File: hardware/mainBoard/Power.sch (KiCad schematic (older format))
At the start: 70 parts

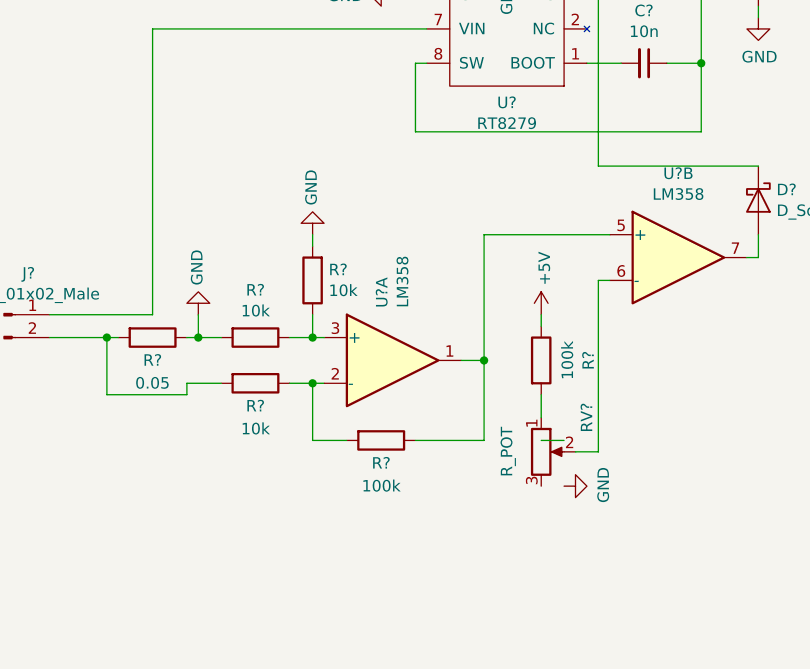
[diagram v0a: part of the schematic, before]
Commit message: Added external connections, analog conditioning and several items
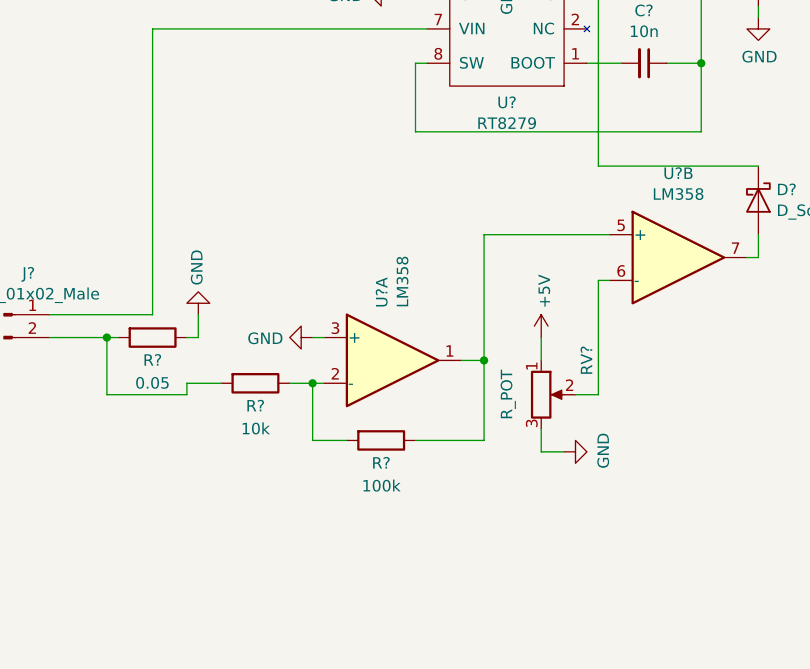
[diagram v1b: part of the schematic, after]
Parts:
- removed R? (x2): 10k, symbol Device:R
- removed R?: 100k, symbol Device:R
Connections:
- net +5V: now also RV?.1
- net GND: now also RV?.3, U?.3 (+)
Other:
- moved on the sheet: RV?
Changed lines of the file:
@@
 EESchema Schematic File Version 4
+LIBS:prockeckv2-cache
 EELAYER 30 0
 EELAYER END
 $Descr A4 11693 8268
 encoding utf-8
-Sheet 5 5
+Sheet 4 8
 Title ""
 Date ""
@@
 	8200 5350 8250 5350
 Wire Wire Line
-	8200 6100 8200 5350
-Wire Wire Line
-	8100 6100 8200 6100
+	8200 5850 8200 5350
+Wire Wire Line
+	8100 5850 8200 5850
 Wire Wire Line
 	6250 4250 7450 4250
-Wire Wire Line
-	7950 5550 7950 5500
-Wire Wire Line
-	7950 5950 7950 5850
-Wire Wire Line
-	8050 6050 7950 6050
 $Comp
 L power:GND #PWR?
 U 1 1 5E4F0960
-P 8050 6250
-F 0 "#PWR?" H 8050 6000 50  0001 C CNN
-F 1 "GND" H 8055 6077 50  0000 C CNN
-F 2 "" H 8050 6250 50  0001 C CNN
-F 3 "" H 8050 6250 50  0001 C CNN
-	1    8050 6250
+P 8050 6100
+F 0 "#PWR?" H 8050 5850 50  0001 C CNN
+F 1 "GND" H 8055 5927 50  0000 C CNN
+F 2 "" H 8050 6100 50  0001 C CNN
+F 3 "" H 8050 6100 50  0001 C CNN
+	1    8050 6100
 	0    -1   -1   0
 $EndComp
@@
 L Device:R_POT RV?
 U 1 1 5E4DE4A3
-P 7950 6100
-F 0 "RV?" V 8150 6250 50  0000 C CNN
-F 1 "R_POT" V 7800 6100 50  0000 C CNN
-F 2 "" H 7950 6100 50  0001 C CNN
-F 3 "~" H 7950 6100 50  0001 C CNN
-	1    7950 6100
-	1    0    0    -1
-$EndComp
-$Comp
-L Device:R R?
-U 1 1 5E4DD69F
-P 7950 5700
-F 0 "R?" V 8157 5700 50  0000 C CNN
-F 1 "100k" V 8066 5700 50  0000 C CNN
-F 2 "" V 7880 5700 50  0001 C CNN
-F 3 "~" H 7950 5700 50  0001 C CNN
-	1    7950 5700
+P 7950 5850
+F 0 "RV?" V 8150 6000 50  0000 C CNN
+F 1 "R_POT" V 7800 5850 50  0000 C CNN
+F 2 "" H 7950 5850 50  0001 C CNN
+F 3 "~" H 7950 5850 50  0001 C CNN
+	1    7950 5850
 	1    0    0    -1
 $EndComp
@@
 L power:+5V #PWR?
 U 1 1 5E4CA2F2
-P 7950 5500
-F 0 "#PWR?" H 7950 5350 50  0001 C CNN
-F 1 "+5V" V 7965 5628 50  0000 L CNN
-F 2 "" H 7950 5500 50  0001 C CNN
-F 3 "" H 7950 5500 50  0001 C CNN
-	1    7950 5500
+P 7950 5600
+F 0 "#PWR?" H 7950 5450 50  0001 C CNN
+F 1 "+5V" V 7965 5728 50  0000 L CNN
+F 2 "" H 7950 5600 50  0001 C CNN
+F 3 "" H 7950 5600 50  0001 C CNN
+	1    7950 5600
 	1    0    0    -1
 $EndComp
@@
 $EndComp
 Wire Wire Line
-	6450 5600 6550 5600
-Connection ~ 6450 5600
-Wire Wire Line
 	6450 5500 6450 5600
 $Comp
@@
 Wire Wire Line
 	5800 5500 6250 5500
-Wire Wire Line
-	6950 5150 6950 5200
 $Comp
 L power:GND #PWR?
 U 1 1 5E346CB4
-P 6950 5150
-F 0 "#PWR?" H 6950 4900 50  0001 C CNN
-F 1 "GND" V 6955 5022 50  0000 R CNN
-F 2 "" H 6950 5150 50  0001 C CNN
-F 3 "" H 6950 5150 50  0001 C CNN
-	1    6950 5150
-	-1   0    0    1
-$EndComp
-Wire Wire Line
-	6950 5600 7000 5600
-Connection ~ 6950 5600
-Wire Wire Line
-	6950 5500 6950 5600
-Wire Wire Line
-	6850 5600 6950 5600
+P 6950 5600
+F 0 "#PWR?" H 6950 5350 50  0001 C CNN
+F 1 "GND" V 6955 5472 50  0000 R CNN
+F 2 "" H 6950 5600 50  0001 C CNN
+F 3 "" H 6950 5600 50  0001 C CNN
+	1    6950 5600
+	0    1    1    0
+$EndComp
 Wire Wire Line
 	6400 5600 6450 5600
@@
 F 3 "~" H 6700 5800 50  0001 C CNN
 	1    6700 5800
-	0    1    1    0
-$EndComp
-$Comp
-L Device:R R?
-U 1 1 5E2DFA45
-P 6950 5350
-F 0 "R?" H 6880 5304 50  0000 R CNN
-F 1 "10k" H 6880 5395 50  0000 R CNN
-F 2 "" V 6880 5350 50  0001 C CNN
-F 3 "~" H 6950 5350 50  0001 C CNN
-	1    6950 5350
-	-1   0    0    1
-$EndComp
-$Comp
-L Device:R R?
-U 1 1 5E2DF58C
-P 6700 5600
-F 0 "R?" V 6493 5600 50  0000 C CNN
-F 1 "10k" V 6584 5600 50  0000 C CNN
-F 2 "" V 6630 5600 50  0001 C CNN
-F 3 "~" H 6700 5600 50  0001 C CNN
-	1    6700 5600
 	0    1    1    0
 $EndComp
@@
 Wire Notes Line
 	3350 3650 7650 3650
+Wire Wire Line
+	7950 5600 7950 5700
+Wire Wire Line
+	8050 6100 7950 6100
+Wire Wire Line
+	7950 6100 7950 6000
+Wire Wire Line
+	6950 5600 7000 5600
 $EndSCHEMATC

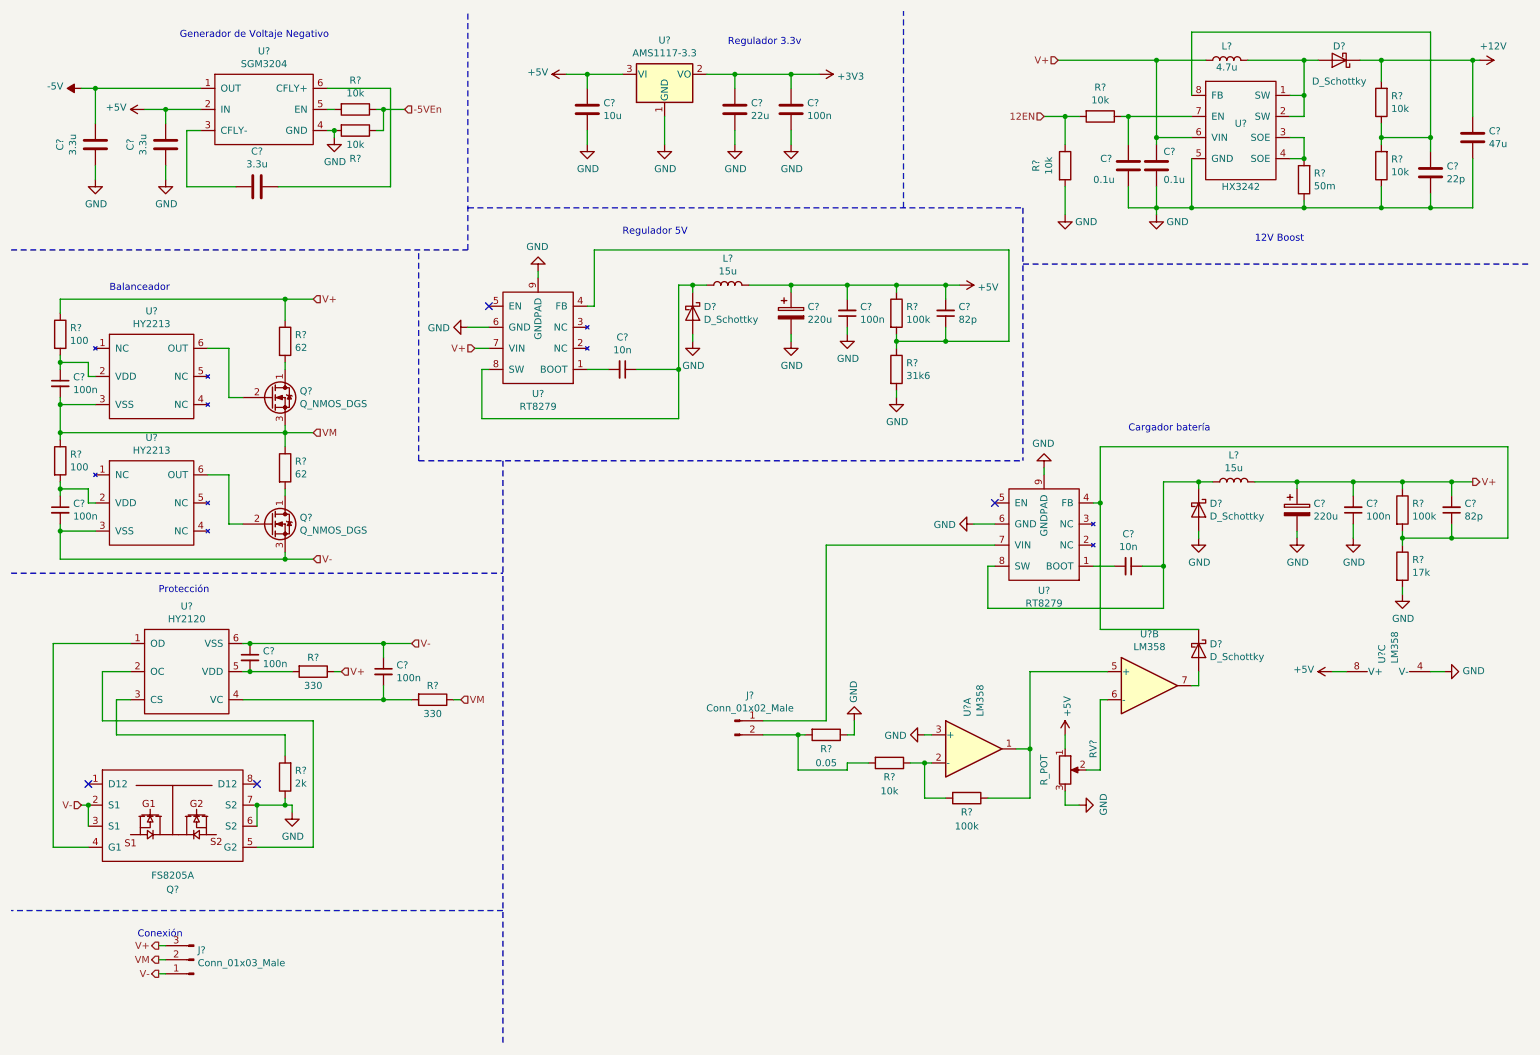
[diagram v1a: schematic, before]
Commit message: Ended schematic, created some pcb footprints
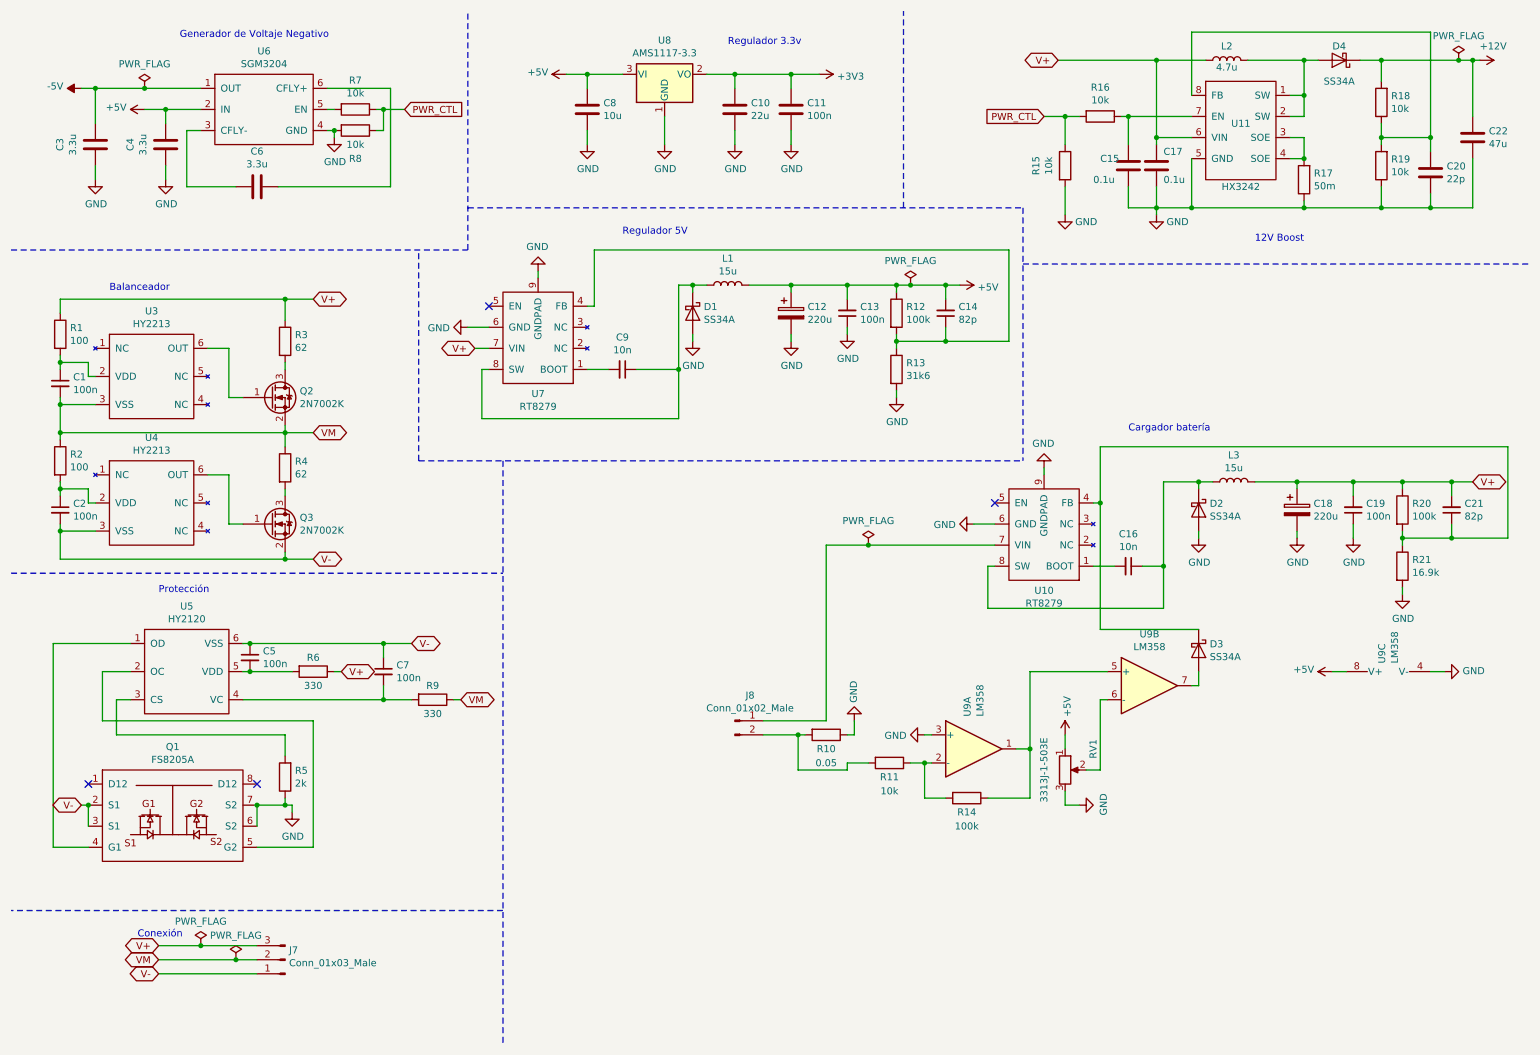
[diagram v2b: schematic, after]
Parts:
- removed Q?: FS8205A, symbol Chinaland:FS8205A
- removed Q? (x2): Q_NMOS_DGS, symbol Device:Q_NMOS_DGS
- added Q1: FS8205A, Package_SO:TSSOP-8_4.4x3mm_P0.65mm, symbol Chinaland:FS8205A
- added Q2, Q3: 2N7002K, Package_TO_SOT_SMD:SOT-23_Handsoldering, symbol Device:Q_NMOS_GSD
- C1, C13, C14, C16, C19, C2, C21, C5, C7, C9: renamed from C?; footprint (none) -> Capacitor_SMD:C_0603_1608Metric_Pad1.05x0.95mm_HandSolder
- C12, C18: renamed from C?; footprint (none) -> Capacitor_SMD:CP_Elec_6.3x5.4
- C8: renamed from C?; footprint Capacitor_SMD:C_0805_2012Metric_Pad1.15x1.40mm_HandSolder -> Capacitor_SMD:C_0603_1608Metric_Pad1.05x0.95mm_HandSolder
- D1, D2, D3: renamed from D?; value D_Schottky -> SS34A; footprint (none) -> Diode_SMD:D_SMA
- D4: renamed from D?; value D_Schottky -> SS34A
- J7: renamed from J?; footprint (none) -> Connector_JST:JST_EH_B3B-EH-A_1x03_P2.50mm_Vertical
- J8: renamed from J?; footprint (none) -> Connector_JST:JST_EH_B2B-EH-A_1x02_P2.50mm_Vertical
- L1: renamed from L?; footprint (none) -> chinalandfoot:SLO0630h; MPN (none) -> SLO0630H150MTT
- L3: renamed from L?; footprint (none) -> chinalandfoot:SLO0630h
- R1, R10, R11, R12, R13, R14, R2, R20, R3, R4, R5, R6, R9: renamed from R?; footprint (none) -> Resistor_SMD:R_0603_1608Metric_Pad1.05x0.95mm_HandSolder
- R21: renamed from R?; value 17k -> 16.9k; footprint (none) -> Resistor_SMD:R_0603_1608Metric_Pad1.05x0.95mm_HandSolder
- RV1: renamed from RV?; value R_POT -> 3313J-1-503E; footprint (none) -> chinalandfoot:Bourns 3313J
- U10, U7: renamed from U?; footprint (none) -> Package_SO:SOIC-8-1EP_3.9x4.9mm_P1.27mm_EP2.514x3.2mm_ThermalVias
- U3, U5: renamed from U?; footprint (none) -> Package_TO_SOT_SMD:SOT-23-6_Handsoldering
- U4: renamed from U?; footprint (none) -> Package_TO_SOT_SMD:SOT-23-6_Handsoldering; MPN (none) -> HY2213-BB3A
- U9: renamed from U?; footprint (none) -> Package_SO:SOIC-8_3.9x4.9mm_P1.27mm
- gave numbers to parts that had none: 20
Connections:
- net 12EN is gone; now on net PWR_CTL: R15.1, R16.2
- net GND: now also Q1.6 (S2), Q1.7 (S2)
- net V-: now also Q1.2 (S1), Q1.3 (S1), Q3.2 (S)
- net VM: now also Q2.2 (S)
- net at U3.6 (OUT): now also Q2.1 (G)
- net at U4.6 (OUT): now also Q3.1 (G)
- net at U5.1 (OD): now also Q1.4 (G1)
- net at U5.2 (OC): now also Q1.5 (G2)
- net at R3.2: now also Q2.3 (D)
- net at R4.2: now also Q3.3 (D)
- net -5VEn renamed PWR_CTL
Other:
- moved on the sheet: J7

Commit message: First working software
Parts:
- C1, C10, C11, C13, C14, C16, C19, C2, C20, C21, C22, C3, C4, C5, C6, C7, C9: URL (none) -> https://lcsc.com/product-detail/Multilayer-Ceramic-Capacito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
- C12, C18: URL (none) -> https://lcsc.com/product-detail/Others_ROQANG-RT1A221M0605_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
- C15, C17: value 0.1u -> 100n; URL (none) -> https://lcsc.com/product-detail/Multilayer-Ceramic-Capacito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
- C8: URL (none) -> https://lcsc.com/product-detail/Others_Samsung-Electro-Mech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
- D1, D2, D3, D4: URL (none) -> https://lcsc.com/product-detail/Schottky-Barrier-Diodes-SBD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
- L1, L3: URL (none) -> https://lcsc.com/product-detail/Power-Inductors_Sunltech-Te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
- L2: URL (none) -> https://lcsc.com/product-detail/Power-Inductors_Taiyo-Yuden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
- Q1: URL (none) -> https://lcsc.com/product-detail/MOSFET_Fortune-Semicon-8205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
- R1, R12, R13, R14, R17, R2, R20, R21, R6, R9: URL (none) -> https://lcsc.com/product-detail/Chip-Resistor-Surface-Mount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
- R10: value 0.05 -> 50m; URL (none) -> https://lcsc.com/product-detail/Chip-Resistor-Surface-Mount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
- R11, R15, R16, R18, R19, R7, R8: URL (none) -> https://lcsc.com/product-detail/New-Arrivals_SANYEAR-SY0603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
- R3, R4: value 62 -> 100; URL (none) -> https://lcsc.com/product-detail/Chip-Resistor-Surface-Mount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
- R5: value 2k -> 2k2; URL (none) -> https://lcsc.com/product-detail/Chip-Resistor-Surface-Mount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
- RV1: URL (none) -> https://lcsc.com/product-detail/Precision-Potentiometer_BOU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
- U10, U7: URL (none) -> https://lcsc.com/product-detail/DC-DC-Converters_RT8279GSP_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
- U11: URL (none) -> https://lcsc.com/product-detail/DC-DC-Converters_HEXIN-HX32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
- U3, U4: URL (none) -> https://lcsc.com/product-detail/PMIC-Battery-Management_HYC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
- U5: URL (none) -> https://lcsc.com/product-detail/Battery-Protection-ICs_HYCO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
- U6: URL (none) -> https://lcsc.com/product-detail/DC-DC-Converters_SGMICRO-SG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
- U9: URL (none) -> https://lcsc.com/product-detail/Others_IDCHIP-LM358_C329455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
